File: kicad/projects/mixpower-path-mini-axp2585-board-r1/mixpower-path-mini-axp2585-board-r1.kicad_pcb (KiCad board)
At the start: 4 copper layers, 28 x 50.8 mm, 87 parts, among them J1 USB_C_USB2.0_16P, J2 BAT, J2 DATA_HEADER, J3 DATA_CONN, J4 PWR_HEADER, J5 DATA_HEADER, Q1 NTLJS7D2P02P8Z, Q2 NTLJS7D2P02P8Z, Q3 NTLJS7D2P02P8Z, Q4 Si1539CDL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

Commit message: feat: add production files
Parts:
- R11: value 4.7M -> 1M
- R14, R18, R3, R4: value 4.7k -> 10k
- R15: value 100k -> 806k
- R16: value 1M -> 4.7M
- R17: value 100k -> 91k
- U1: value MIC5219-3.3YM5 -> RT9080

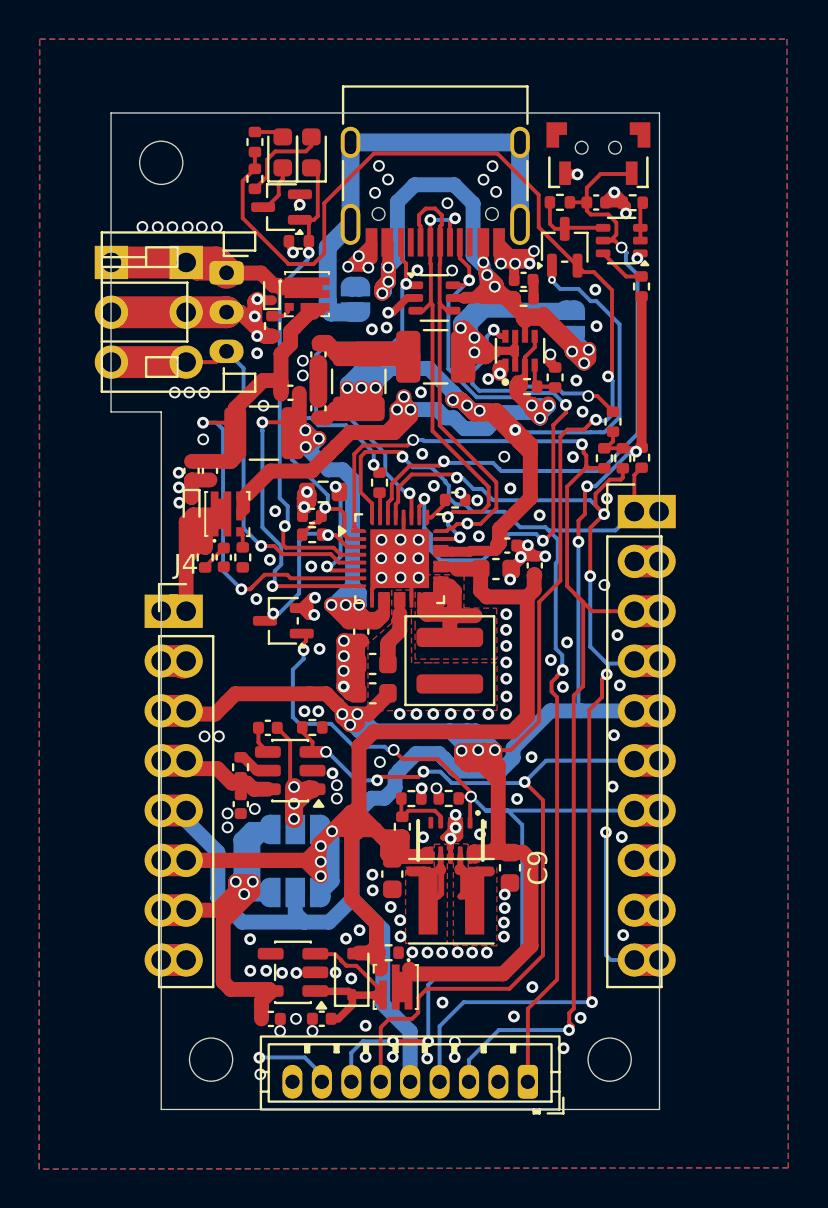
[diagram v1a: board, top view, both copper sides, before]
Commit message: feat: small PCB and (even smaller) schem adjustments
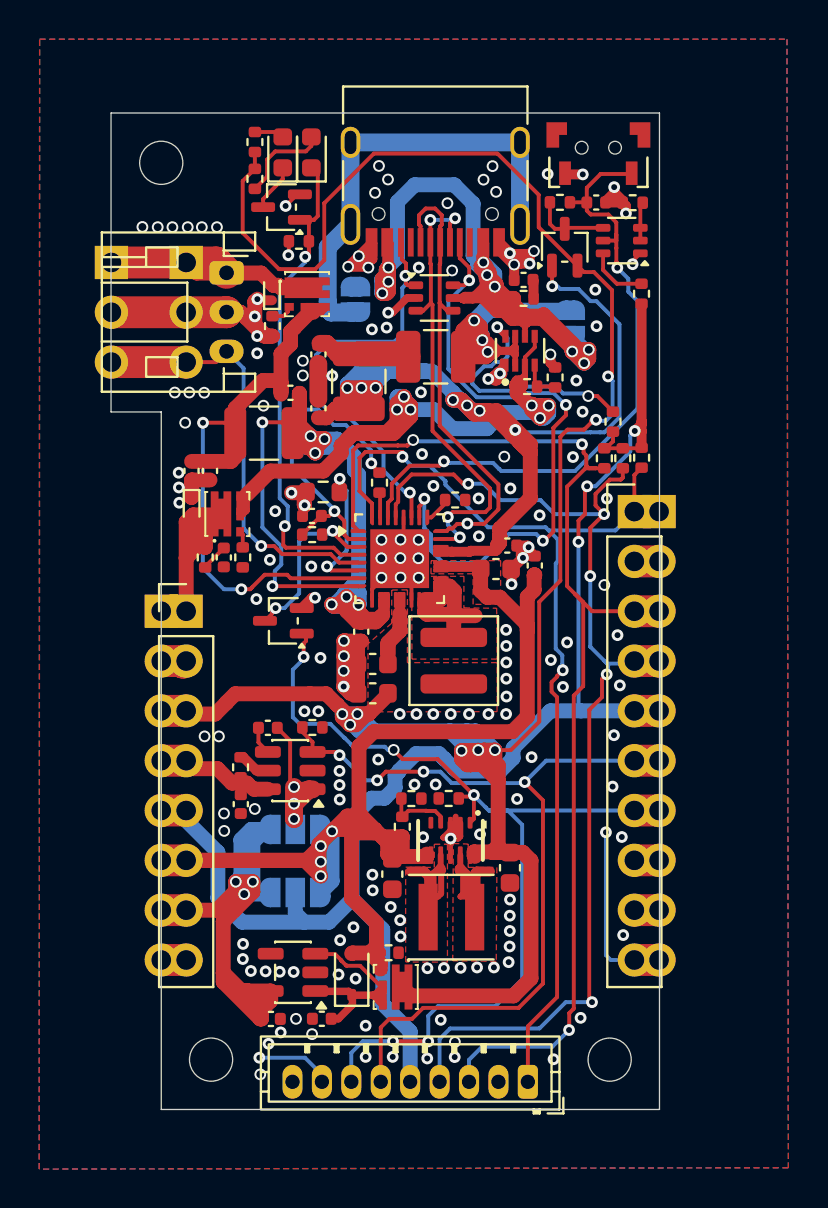
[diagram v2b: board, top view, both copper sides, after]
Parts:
- moved L1 0.81 mm to (209.1, 86.7)
- moved R10 0.37 mm to (218.8, 54.9)
- moved L2 0.20 mm to (209.2, 73.6)
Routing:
- net /VBUS: track 57.6 -> 69.2 mm
- net /BC_BAT: track 48.0 -> 55.9 mm
- net /VEXT: track 37.7 -> 45.2 mm
- net /3V3: track 27.5 -> 31.9 mm
- net /VMUX_PRE: track 21.7 -> 25.6 mm
- net /VSYS: track 118.0 -> 121.6 mm
- net /VCC: track 74.8 -> 77.3 mm
- net /VMUX: track 64.6 -> 67.0 mm
- net GND: track 68.5 -> 70.7 mm, vias 171 -> 166
- net /BC_GPADC: track 6.34 -> 7.69 mm
- net /MUX_ST: track 48.0 -> 48.9 mm
- net /PWRON: track 34.5 -> 33.6 mm
- net /BTN: track 2.45 -> 3.10 mm
- net /D+: track 91.2 -> 90.6 mm
- net /D-: track 88.9 -> 88.4 mm, vias 4 -> 5
- added copper zone on F.Cu, net /5V

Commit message: feat: small adjustments to PCB and schem
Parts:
- added FID1: Fiducial, Fiducial:Fiducial_0.5mm_Mask1mm, F.Cu at (197.6, 47.0)
- added FID2: Fiducial, Fiducial:Fiducial_0.5mm_Mask1mm, F.Cu at (218.4, 91.2)
- added FID3: Fiducial, Fiducial:Fiducial_0.5mm_Mask1mm, F.Cu at (195.6, 91.2)
- added R27: 5.1k, Resistor_SMD:R_0402_1005Metric, B.Cu at (207.8, 55.4)
- added R28: 5.1k, Resistor_SMD:R_0402_1005Metric, B.Cu at (207.8, 57.5)
- moved C21 0.15 mm to (201.8, 66.3)
- moved R25 0.14 mm to (201.9, 67.2)
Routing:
- net /5V: track 74.1 -> 78.8 mm
- net /BC_BAT: track 55.9 -> 60.3 mm
- net /VBUS: track 69.2 -> 72.5 mm
- net /VEXT: track 45.2 -> 48.2 mm
- net /3V3_VIN: track 11.4 -> 13.3 mm
- net /VMUX: track 67.0 -> 68.8 mm
- net GND: track 70.7 -> 72.2 mm, vias 166 -> 170
- net /5VREG_L1: track 6.48 -> 5.25 mm
- net /BC_OTG: track 8.67 -> 9.67 mm
- net /5VREG_L2: track 6.31 -> 5.55 mm
- net /USBC_CC2: track 21.7 -> 22.4 mm
- net /USBC_CC1: track 33.0 -> 33.6 mm
- net /CHG_VLDO: track 16.4 -> 17.1 mm
- net /BAT_TS: track 22.1 -> 22.7 mm
